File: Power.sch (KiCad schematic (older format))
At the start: 38 parts, among them IC1 INA181, IC2 INA181, IC3 INA181, U2 IRS2186, U3 IRS2186, U4 IRS2186

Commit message: - rescued schematic - added *.sch-bak to ignore - fixed bypass diode polarity - fixed PDEN being low - added 0R resistors instead of USB iso option - added caps to DCDC - added filter to VDDA
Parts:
- C20, C21, C22, C23, C24, C25, C26, C27, C28, C29, C30, C31, C32, C37, C38: symbol Device:C -> HSWR-V2-rescue:C-Device
- D4, D5, D6: symbol Device:D_Small -> HSWR-V2-rescue:D_Small-Device
- IC1, IC2, IC3: symbol HSWR-V2-rescue:INA181-Auktoralib -> Amplifier_Current:INA181
- R21, R24, R25: symbol Device:R_Small -> HSWR-V2-rescue:R_Small-Device
- R26, R27, R32, R33, R34, R35, R36, R37, R38, R39, R40: symbol Device:R -> HSWR-V2-rescue:R-Device
- U2, U3, U4: symbol HSWR-V2-rescue:IRS2186-Driver_FET -> Driver_FET:IRS2186
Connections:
- wire segments 70 -> 75
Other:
- moved on the sheet: C20, C21, C22, C24, C25, C26, C27, C28, C29, C30, C31, C32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

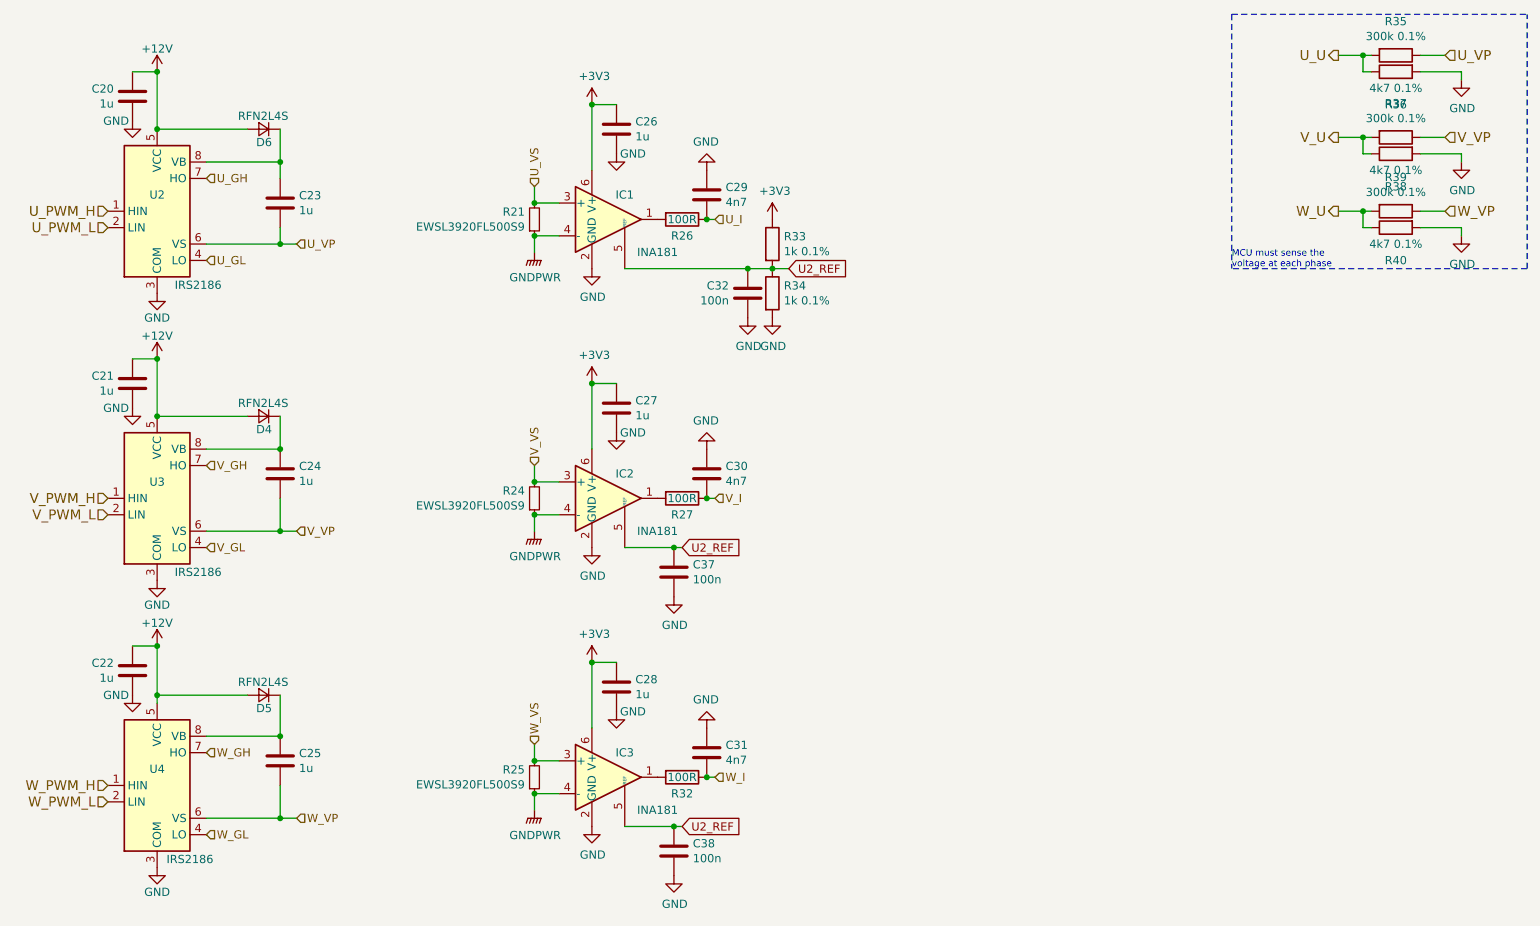
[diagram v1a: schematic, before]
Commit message: - changed CSA for Hall effect sensors - updated power stage layout
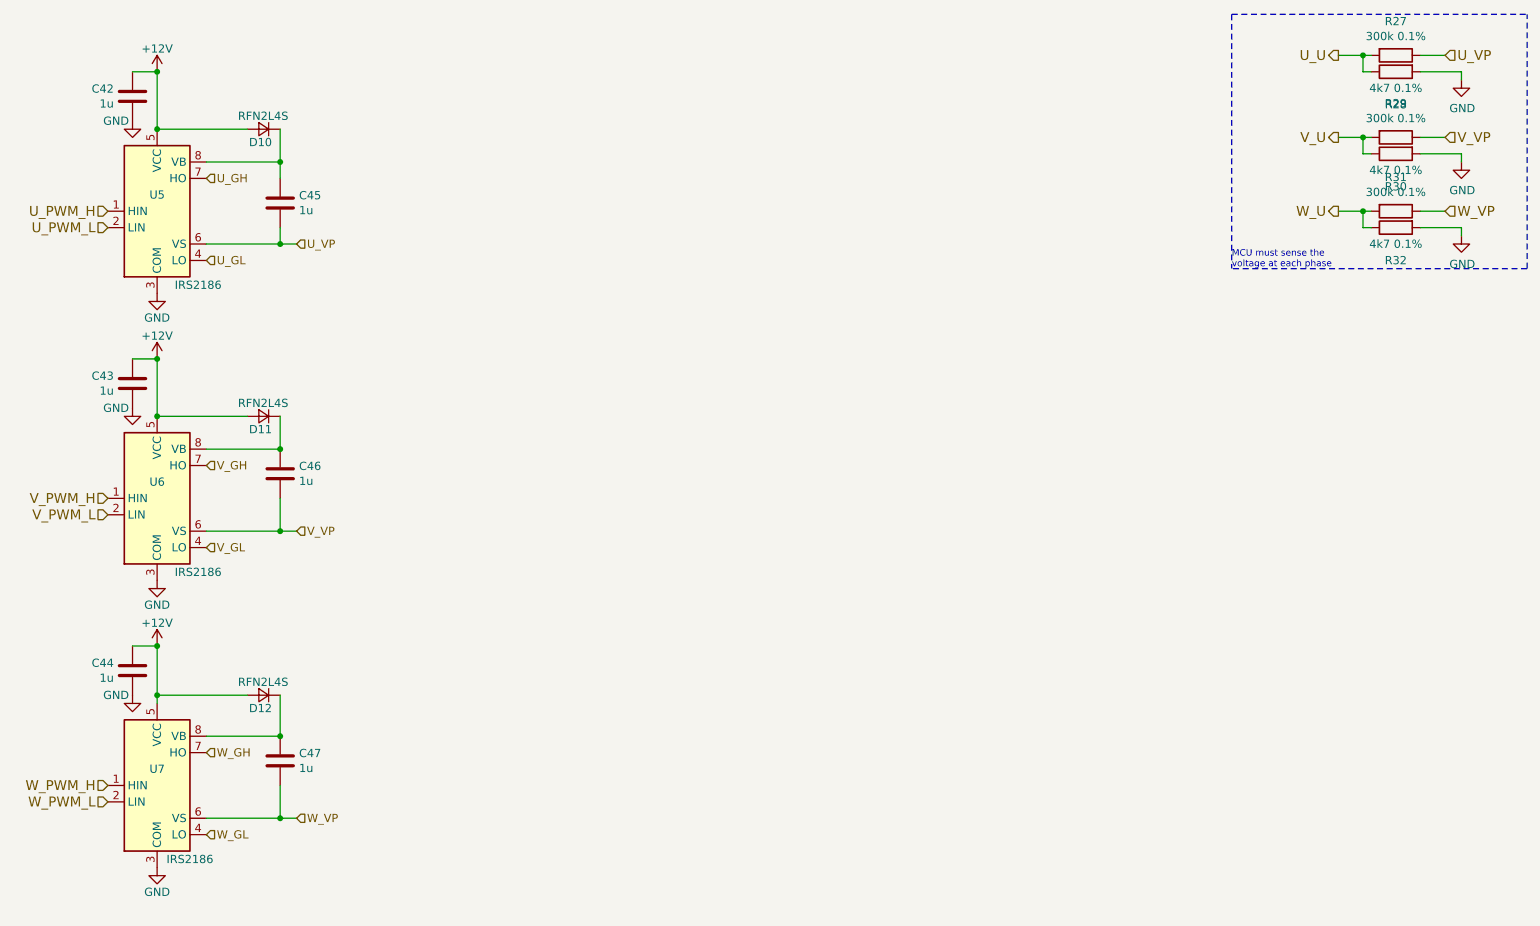
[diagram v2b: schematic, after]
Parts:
- removed C26, C27, C28: 1u, Capacitor_SMD:C_0805_2012Metric, symbol HSWR-V2-rescue:C-Device
- removed C29, C30, C31: 4n7, Capacitor_SMD:C_0805_2012Metric, symbol HSWR-V2-rescue:C-Device
- removed C32, C37, C38: 100n, Capacitor_SMD:C_0805_2012Metric, symbol HSWR-V2-rescue:C-Device
- removed IC1, IC2, IC3: INA181, Package_TO_SOT_SMD:SOT-23-6, symbol Amplifier_Current:INA181
- removed R21, R24, R25: EWSL3920FL500S9, Resistor_SMD:R_4020_10251Metric, symbol HSWR-V2-rescue:R_Small-Device
- removed R26, R27, R32: 100R, Resistor_SMD:R_0805_2012Metric, symbol HSWR-V2-rescue:R-Device
- removed R33, R34: 1k 0.1%, Resistor_SMD:R_0805_2012Metric, symbol HSWR-V2-rescue:R-Device
- renumbered C20 to C42, C21 to C43, C22 to C44, C23 to C45, C24 to C46, C25 to C47, D6 to D10, D4 to D11, D5 to D12, R35 to R27, R36 to R28, R37 to R29, R38 to R30, R39 to R31, R40 to R32, U2 to U5, U3 to U6, U4 to U7

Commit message: - removed rescue lib and symbols - added HSWR.lib
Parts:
- C42, C43, C44, C45, C46, C47: symbol HSWR-V2-rescue:C-Device -> Device:C
- D10, D11, D12: symbol HSWR-V2-rescue:D_Small-Device -> Device:D_Small
- R27, R28, R29, R30, R31, R32: symbol HSWR-V2-rescue:R-Device -> Device:R
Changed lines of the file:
@@
 $Descr A4 11693 8268
 encoding utf-8
-Sheet 5 8
+Sheet 8 8
 Title "HSWR MOSFET Driver"
 Date "2017-02-05"
@@
 	10800 2450 10800 900
 $Comp
-L HSWR-V2-rescue:D_Small-Device D10
+L Device:D_Small D10
 U 1 1 574EBB78
 P 3100 1600
@@
 $EndComp
 $Comp
-L HSWR-V2-rescue:+12V-power #PWR086
+L power:+12V #PWR086
 U 1 1 574ED597
 P 2450 1250
+AR Path="/574ED597" Ref="#PWR086"  Part="1"
+AR Path="/5895E6A0/574ED597" Ref="#PWR086"  Part="1"
 F 0 "#PWR086" H 2450 1100 50  0001 C CNN
 F 1 "+12V" H 2450 1390 50  0000 C CNN
@@
 $EndComp
 $Comp
-L HSWR-V2-rescue:GND-power #PWR087
+L power:GND #PWR087
 U 1 1 574F0470
 P 2450 2600
@@
 	1    0    0    -1
 $EndComp
-$Comp
-L HSWR-V2-rescue:C-Device C45
-U 1 1 5CA05A73
-P 3200 2050
-F 0 "C45" H 3315 2096 50  0000 L CNN
-F 1 "1u" H 3315 2005 50  0000 L CNN
-F 2 "Capacitor_SMD:C_0805_2012Metric" H 3238 1900 50  0001 C CNN
-F 3 "~" H 3200 2050 50  0001 C CNN
-	1    3200 2050
-	1    0    0    -1
-$EndComp
 Wire Wire Line
 	3200 1600 3200 1800
@@
 	3000 1600 2450 1600
 $Comp
-L HSWR-V2-rescue:GND-power #PWR083
+L power:GND #PWR083
 U 1 1 574EDDD7
 P 2300 1550
@@
 $EndComp
 $Comp
-L HSWR-V2-rescue:C-Device C42
+L Device:C C42
 U 1 1 5CA15C56
 P 2300 1400
@@
 Wire Wire Line
 	2450 1600 2450 1250
-Connection ~ 2450 1250
 Wire Notes Line
 	9000 900  10800 900
@@
 	10800 2450 9000 2450
 $Comp
-L HSWR-V2-rescue:R-Device R27
+L Device:R R27
 U 1 1 5CA6D089
 P 10000 1150
@@
 $EndComp
 $Comp
-L HSWR-V2-rescue:R-Device R28
+L Device:R R28
 U 1 1 5CA6D0E6
 P 10000 1250
@@
 $EndComp
 $Comp
-L HSWR-V2-rescue:R-Device R29
+L Device:R R29
 U 1 1 5CA727D2
 P 10000 1650
@@
 $EndComp
 $Comp
-L HSWR-V2-rescue:R-Device R30
+L Device:R R30
 U 1 1 5CA72804
 P 10000 1750
@@
 $EndComp
 $Comp
-L HSWR-V2-rescue:R-Device R31
+L Device:R R31
 U 1 1 5CA72B3A
 P 10000 2100
@@
 $EndComp
 $Comp
-L HSWR-V2-rescue:R-Device R32
+L Device:R R32
 U 1 1 5CA72B6E
 P 10000 2200
@@
 W_VP
 $Comp
-L HSWR-V2-rescue:GND-power #PWR092
+L power:GND #PWR092
 U 1 1 5CA72D49
 P 10400 1300
@@
 $EndComp
 $Comp
-L HSWR-V2-rescue:GND-power #PWR093
+L power:GND #PWR093
 U 1 1 5CA72D7F
 P 10400 1800
@@
 $EndComp
 $Comp
-L HSWR-V2-rescue:GND-power #PWR094
+L power:GND #PWR094
 U 1 1 5CA72EE0
 P 10400 2250
@@
 $EndComp
 $Comp
-L HSWR-V2-rescue:D_Small-Device D11
+L Device:D_Small D11
 U 1 1 5CA74625
 P 3100 3350
@@
 $EndComp
 $Comp
-L HSWR-V2-rescue:+12V-power #PWR088
+L power:+12V #PWR088
 U 1 1 5CA7462B
 P 2450 3000
+AR Path="/5CA7462B" Ref="#PWR088"  Part="1"
+AR Path="/5895E6A0/5CA7462B" Ref="#PWR088"  Part="1"
 F 0 "#PWR088" H 2450 2850 50  0001 C CNN
 F 1 "+12V" H 2450 3140 50  0000 C CNN
@@
 $EndComp
 $Comp
-L HSWR-V2-rescue:GND-power #PWR089
+L power:GND #PWR089
 U 1 1 5CA74631
 P 2450 4350
@@
 V_PWM_L
 $Comp
-L HSWR-V2-rescue:C-Device C46
+L Device:C C46
 U 1 1 5CA7463F
 P 3200 3700
@@
 Wire Wire Line
 	3200 3350 3200 3550
-Connection ~ 3200 3550
 Wire Wire Line
 	3000 3350 2450 3350
 $Comp
-L HSWR-V2-rescue:GND-power #PWR084
+L power:GND #PWR084
 U 1 1 5CA7464A
 P 2300 3300
@@
 $EndComp
 $Comp
-L HSWR-V2-rescue:C-Device C43
+L Device:C C43
 U 1 1 5CA74650
 P 2300 3150
@@
 Wire Wire Line
 	2450 3350 2450 3000
-Connection ~ 2450 3000
-$Comp
-L HSWR-V2-rescue:D_Small-Device D12
+$Comp
+L Device:D_Small D12
 U 1 1 5CA759F0
 P 3100 5050
@@
 $EndComp
 $Comp
-L HSWR-V2-rescue:+12V-power #PWR090
+L power:+12V #PWR090
 U 1 1 5CA759F6
 P 2450 4750
+AR Path="/5CA759F6" Ref="#PWR090"  Part="1"
+AR Path="/5895E6A0/5CA759F6" Ref="#PWR090"  Part="1"
 F 0 "#PWR090" H 2450 4600 50  0001 C CNN
 F 1 "+12V" H 2450 4890 50  0000 C CNN
@@
 $EndComp
 $Comp
-L HSWR-V2-rescue:GND-power #PWR091
+L power:GND #PWR091
 U 1 1 5CA759FC
 P 2450 6100
@@
 $EndComp
 $Comp
-L HSWR-V2-rescue:C-Device C47
+L Device:C C47
 U 1 1 5CA75A0A
 P 3200 5450
@@
 	3000 5050 2450 5050
 $Comp
-L HSWR-V2-rescue:GND-power #PWR085
+L power:GND #PWR085
 U 1 1 5CA75A15
 P 2300 5050
@@
 $EndComp
 $Comp
-L HSWR-V2-rescue:C-Device C44
+L Device:C C44
 U 1 1 5CA75A1B
 P 2300 4900
@@
 Wire Wire Line
 	2450 5100 2450 5050
-Connection ~ 2450 4750
 Connection ~ 2450 1600
 Wire Wire Line
@@
 Wire Wire Line
 	2750 5300 3200 5300
-Connection ~ 3200 5300
 Wire Wire Line
 	3200 5600 3200 5800
@@
 	3200 5800 2750 5800
 Connection ~ 3200 5800
+$Comp
+L Device:C C45
+U 1 1 5CA05A73
+P 3200 2050
+F 0 "C45" H 3315 2096 50  0000 L CNN
+F 1 "1u" H 3315 2005 50  0000 L CNN
+F 2 "Capacitor_SMD:C_0805_2012Metric" H 3238 1900 50  0001 C CNN
+F 3 "~" H 3200 2050 50  0001 C CNN
+	1    3200 2050
+	1    0    0    -1
+$EndComp
+Connection ~ 2450 1250
+Connection ~ 2450 3000
+Connection ~ 2450 4750
 $EndSCHEMATC
